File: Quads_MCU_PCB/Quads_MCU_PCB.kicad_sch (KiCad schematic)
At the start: 87 parts, among them J1 USB_C_Receptacle_USB2.0_16P, J2 Conn_01x06_Pin, J3 Conn_01x02_Pin, J4 Conn_01x03_Pin, J5 Conn_01x03_Pin, J6 Conn_01x03_Pin, J7 Conn_01x03_Pin, SW1 SW_Push, U1 STM32H723ZGTx, U3 ISOW1044, U4 TSR_1-2450, U5 AP7361C-33E, U6 ISOW1044, U7 ISOW1044, U8 MCP2518FD-xQBB, U9 ISOW1044, Y1 40MHz, Y2 25MHz

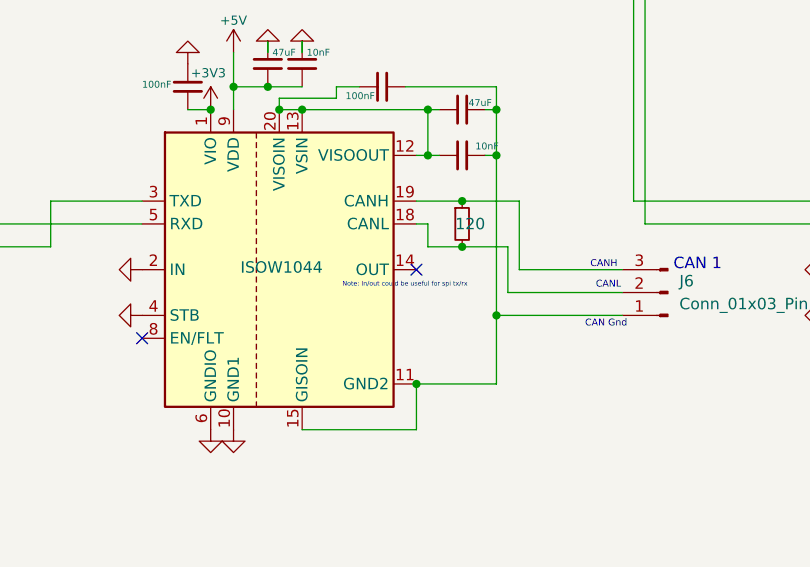
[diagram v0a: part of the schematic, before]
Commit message: Removed old text
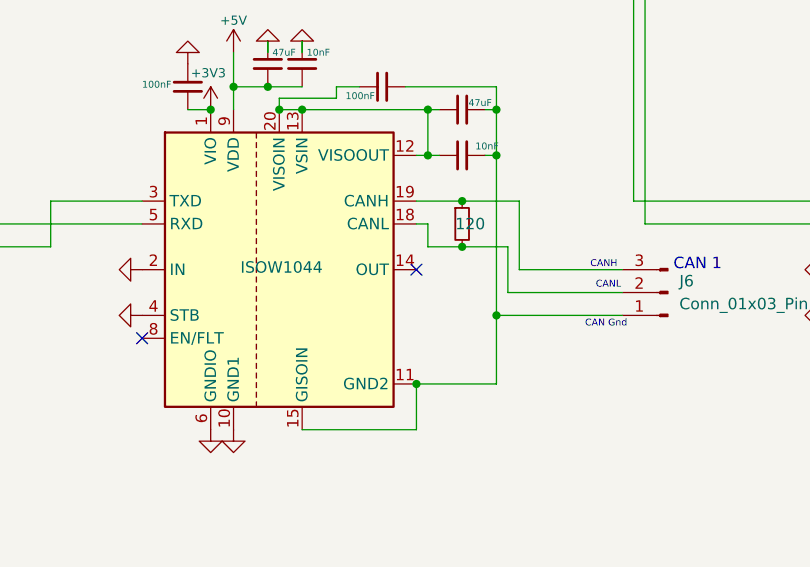
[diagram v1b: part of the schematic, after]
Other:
- note removed: "Note: In/out could be useful for spi tx/rx"
